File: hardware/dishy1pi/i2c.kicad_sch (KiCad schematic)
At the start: 19 parts, among them CN4 KF2EDGR-2.54-4P, CN5 KF2EDGR-2.54-4P, U6 LTC4311ISC6#TRPBF, U7 ISO1540DR, U8 LM75BIMX-5/NOPB

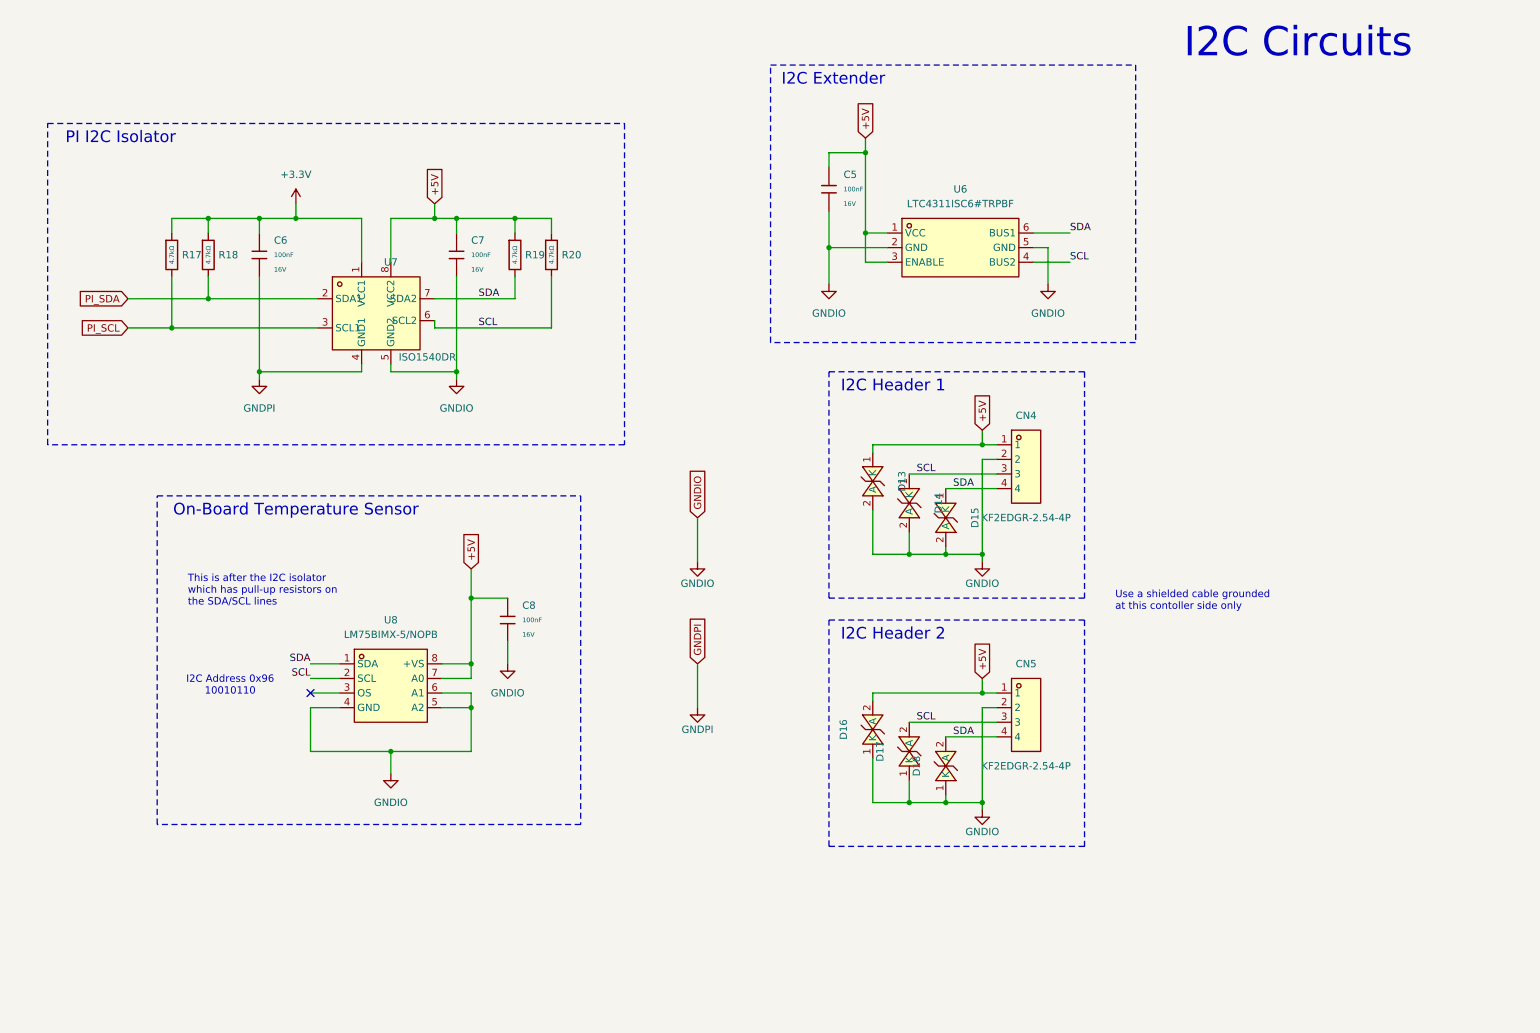
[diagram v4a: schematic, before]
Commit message: Added 12V power input
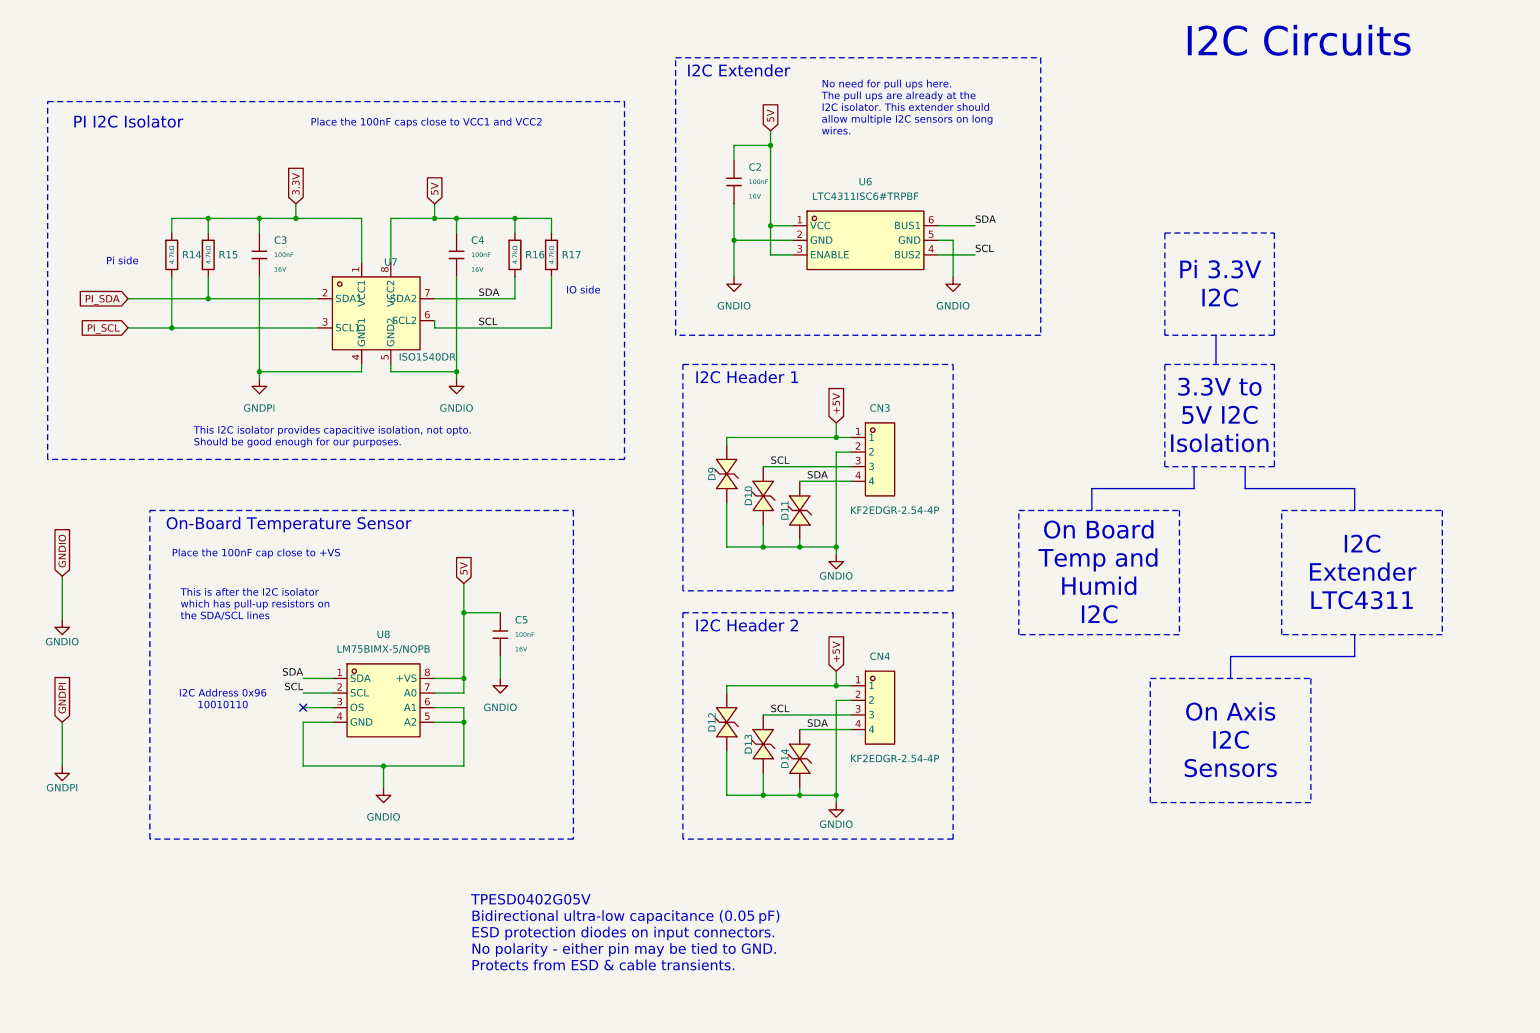
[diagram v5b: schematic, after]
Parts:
- renumbered C5 to C2, C6 to C3, C7 to C4, C8 to C5, CN4 to CN3, CN5 to CN4, D14 to D10, D15 to D11, D16 to D12, D17 to D13, D18 to D14, D13 to D9, R17 to R14, R18 to R15, R19 to R16, R20 to R17
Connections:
- net +5V: no longer C2.1, C4.1, C5.1, R16.1, R17.1, U6.1 (VCC), U6.3 (ENABLE), U7.8 (VCC2), U8.7 (A0), U8.8 (+VS)
- net +3.3V renamed 3.3V
- new net 5V: C2.1, C4.1, C5.1, R16.1, R17.1, U6.1 (VCC), U6.3 (ENABLE), U7.8 (VCC2), U8.7 (A0), U8.8 (+VS)
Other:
- note added: "IO side"
- note added: "No need for pull ups here. The pull ups are already at the I2C isolator. This extender should allow multiple I2C sensors on long wires."
- note added: "Pi side"
- note added: "Place the 100nF cap close to +VS"
- note added: "Place the 100nF caps close to VCC1 and VCC2"
- note added: "TPESD0402G05V Bidirectional ultra-low capacitance (0.05 pF) ESD protection diodes on input connectors. No polarity - either pin may be tied to GND. Protects from ESD & cable transients."
- note added: "This I2C isolator provides capacitive isolation, not opto. Should be good enough for our purposes."
- note removed: "Use a shielded cable grounded at this contoller side only"
- moved on the sheet: C2, C5, CN3, CN4, U6, U8

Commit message: Pushed latest parts lib
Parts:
- added CN7: SM04B-SRSS-TB (LF)(SN), MyParts:CONN-SMD_4P-P1.00_SM04B-SRSS-TB-LF-SN, symbol MyParts:SM04B-SRSS-TB(LF)(SN)
- added R36, R37: 4.7kΩ, PCM_JLCPCB:R_0402, symbol PCM_JLCPCB-Resistors:0402,4.7kΩ
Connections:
- net GNDPI: now also CN7.1, CN7.5, CN7.6
- net 3.3V renamed 3.3V_MCU
- net PI_SCL renamed SCL_MCU
- net PI_SDA renamed SDA_MCU
- new net 3.3V_PI: CN7.2, R36.1, R37.1
- new net SCL_PI: CN7.4, R36.2
- new net SDA_PI: CN7.3, R37.2
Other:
- note added: "JST_SH4 Female like on Adafruit I2C STEMMA boards Connect to any 3.3V I2C sensor"
- note added: "PI I2C to Extra 3.3V I2C Sensors"
- moved on the sheet: C2, C3, C4, C5, CN3, CN4, R14, R15, R16, R17, U6, U7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
